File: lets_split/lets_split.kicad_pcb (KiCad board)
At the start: 2 copper layers, 113 x 82 mm, 64 parts, among them P1 USB-rewire, P2 USB_OTG, P3 WS2812-Strip, P4 TRRS jack, SW1 SW_PUSH, SW10 SW_PUSH, SW11 SW_PUSH, SW12 SW_PUSH, SW13 SW_PUSH, SW14 SW_PUSH, SW15 SW_PUSH, SW16 SW_PUSH, SW17 SW_PUSH, SW18 SW_PUSH, SW19 SW_PUSH, SW2 SW_PUSH, SW20 SW_PUSH, SW21 SW_PUSH, SW22 SW_PUSH, SW23 SW_PUSH, SW24 SW_PUSH, SW3 SW_PUSH, SW4 SW_PUSH, SW5 SW_PUSH, SW6 SW_PUSH, SW7 SW_PUSH, SW8 SW_PUSH, SW9 SW_PUSH, U1 ArduinoProMicro

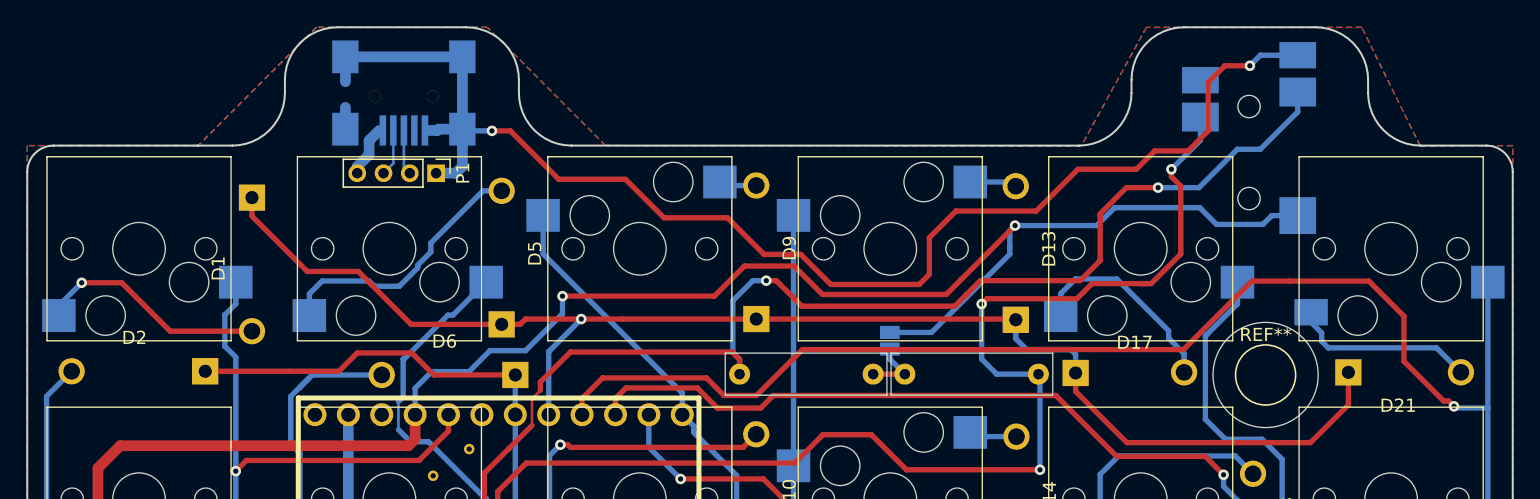
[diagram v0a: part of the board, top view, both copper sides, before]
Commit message: Increased powertraces thickness to TRRS socket
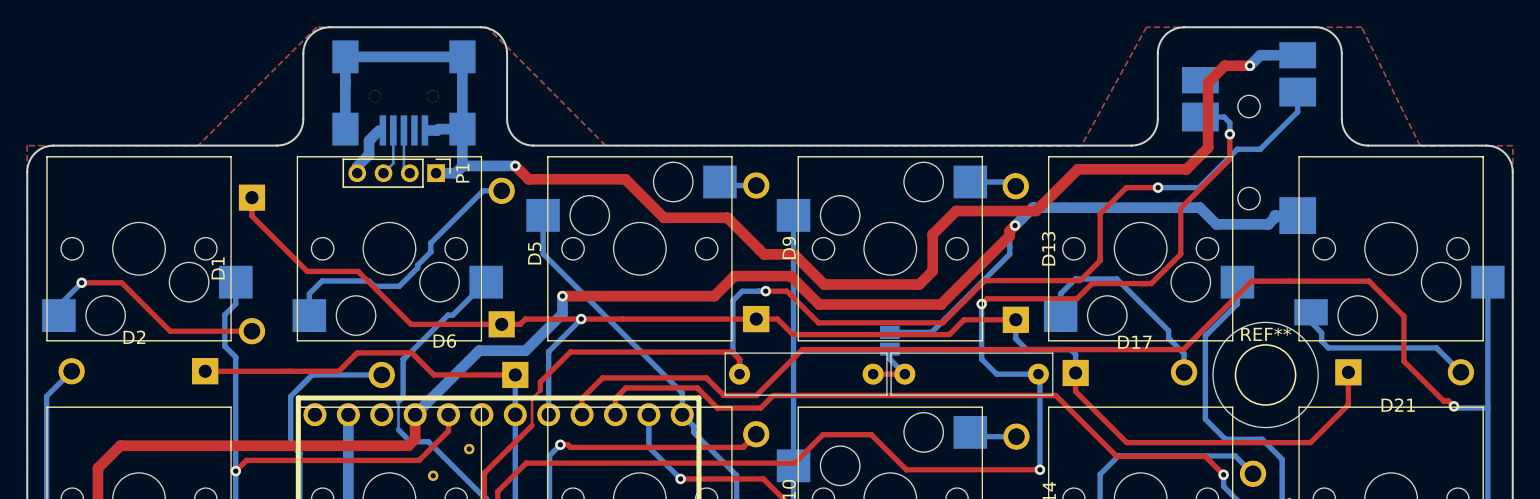
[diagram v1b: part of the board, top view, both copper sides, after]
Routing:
- net SCL/D3: track 99.2 -> 101.5 mm
- net GND: track 143.4 -> 145.2 mm
- net row0: track 106.7 -> 107.7 mm
- net VCC: track 135.3 -> 134.5 mm
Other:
- outline, holes or cut-outs redrawn

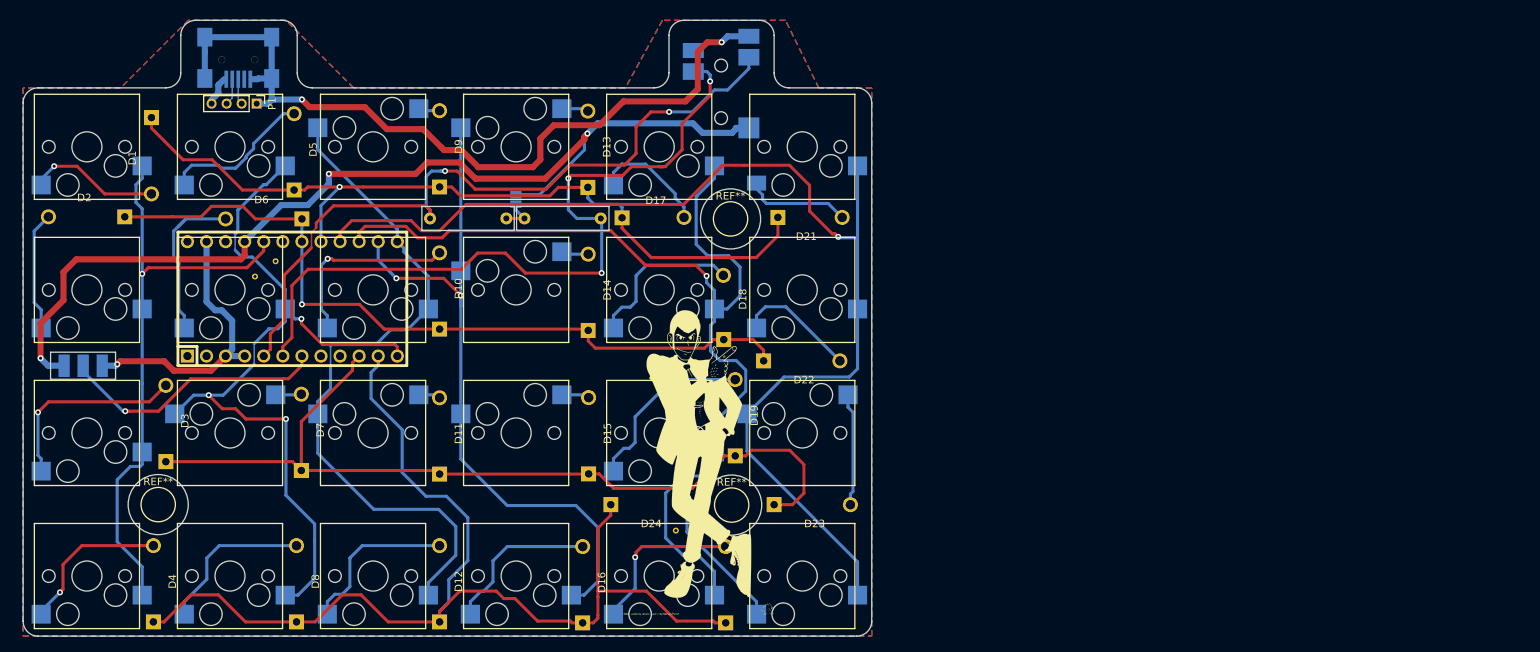
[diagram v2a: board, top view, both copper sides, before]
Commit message: Switched to using diode footprints with actual silk screen, and moved dioes away from socket pads
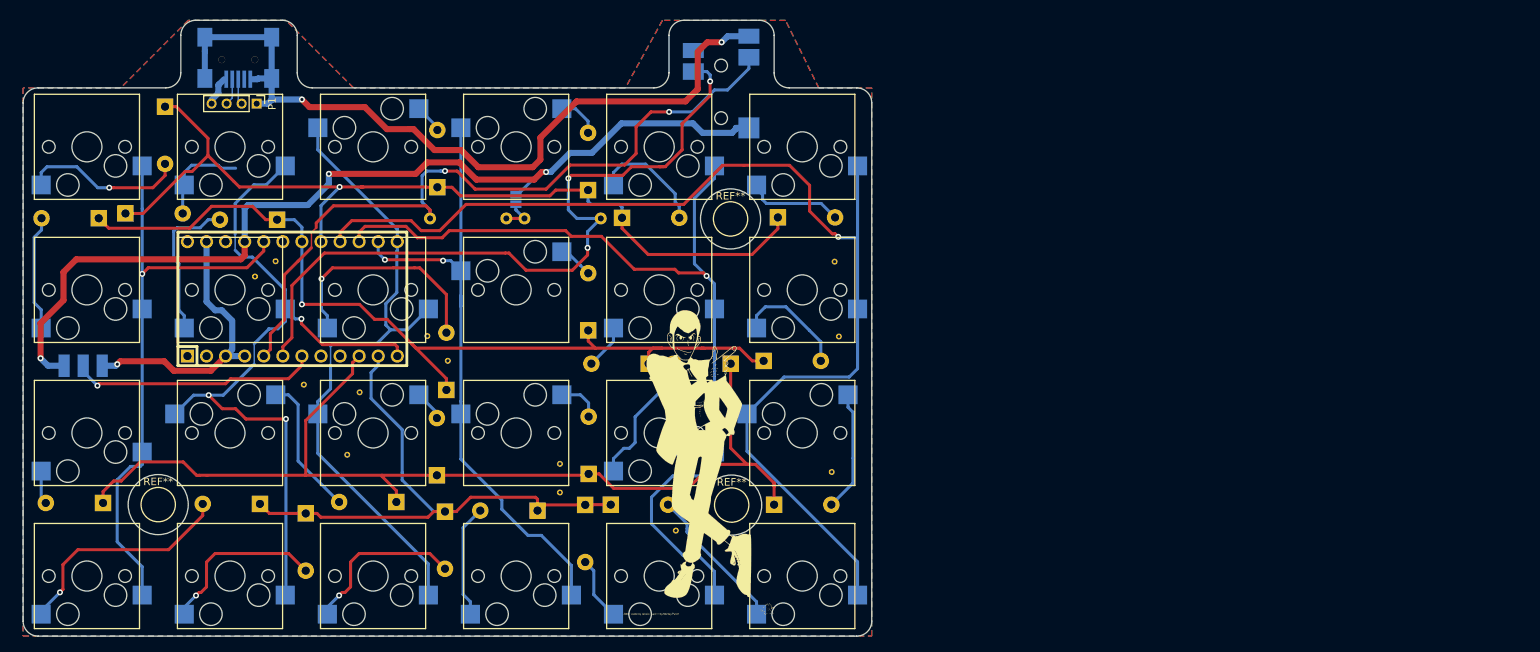
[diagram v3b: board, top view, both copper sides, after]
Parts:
- added REF**: 1pin, Connect:1pin, F.Cu at (135.8, 98.0)
- added REF**: 1pin, Connect:1pin, F.Cu at (153.5, 118.9)
- added REF**: 1pin, Connect:1pin, F.Cu at (190.6, 98.1)
- added REF**: 1pin, Connect:1pin, F.Cu at (138.6, 101.3)
- added REF**: 1pin, Connect:1pin, F.Cu at (119.4, 104.5)
- added REF**: 1pin, Connect:1pin, F.Cu at (126.8, 105.5)
- added REF**: 1pin, Connect:1pin, F.Cu at (125.2, 113.9)
- added REF**: 1pin, Connect:1pin, F.Cu at (189.7, 116.1)
- added REF**: 1pin, Connect:1pin, F.Cu at (190.1, 88.1)
- added REF**: 1pin, Connect:1pin, F.Cu at (153.5, 115.1)
- D1, D10, D11, D12, D13, D14, D15, D16, D17, D18, D19, D2, D20, D21, D22, D23, D24, D3, D4, D5, D6, D7, D8, D9: footprint Diodes_ThroughHole:Diode_DO-41_SOD81_Horizontal_RM10 -> Diodes_ThroughHole:D_DO-41_SOD81_P7.62mm_Horizontal; moved to B.Cu
- P3: footprint SMD_PAD_1x03_Pitch2.54mm -> Wirepads:SMD_PAD_1x03_Pitch2.54mm
- SW6: footprint Kailh-socket -> CherryMX:Kailh-socket
- moved D20 24.4 mm to (156.8, 120.5), turned to 270 degrees
- moved D5 22.7 mm to (95.6, 81.7), turned to 0 degrees
- moved D4 21.2 mm to (113.5, 120.4), turned to 180 degrees
- moved D16 16.1 mm to (150.5, 121.3), turned to 180 degrees
- moved D12 14.7 mm to (138.2, 121.4), turned to 270 degrees
- moved D8 14.5 mm to (119.6, 121.7), turned to 270 degrees
- moved D7 13.3 mm to (131.7, 120.1), turned to 180 degrees
- moved D19 12.3 mm to (176.2, 101.7), turned to 180 degrees
- moved D18 10.5 mm to (165.3, 101.7), turned to 180 degrees
- moved D3 10.0 mm to (92.6, 120.3), turned to 180 degrees
- moved D10 8.15 mm to (138.4, 105.2)
- moved D2 3.47 mm to (92.1, 82.4)
- moved D6 3.30 mm to (115.8, 82.5)
- moved D1 2.33 mm to (100.9, 67.5)
- moved D21 1.60 mm to (182.5, 82.2)
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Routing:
- net row3: track 148.8 -> 76.6 mm
- net Net-(D3-Pad2): track 26.5 -> 4.49 mm, vias 1 -> 0
- net row2: track 116.2 -> 137.8 mm
- net row1: track 103.4 -> 119.5 mm
- net Net-(D18-Pad2): track 21.6 -> 5.96 mm
- net Net-(D7-Pad2): track 3.44 -> 18.8 mm
- net Net-(D20-Pad2): track 21.7 -> 8.51 mm, vias 1 -> 0
- net col4: track 134.1 -> 121.5 mm
- net row0: track 107.7 -> 120.0 mm
- net col3: track 94.4 -> 84.3 mm
- net Net-(D4-Pad2): track 20.9 -> 30.7 mm
- net Net-(D5-Pad2): track 20.4 -> 12.9 mm
- net Net-(D19-Pad2): track 24.2 -> 18.0 mm
- net VCC: track 134.5 -> 128.3 mm
- net Net-(D16-Pad2): track 21.3 -> 15.1 mm
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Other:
- board text removed: "top up"

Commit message: Moved silkscreen around a bit
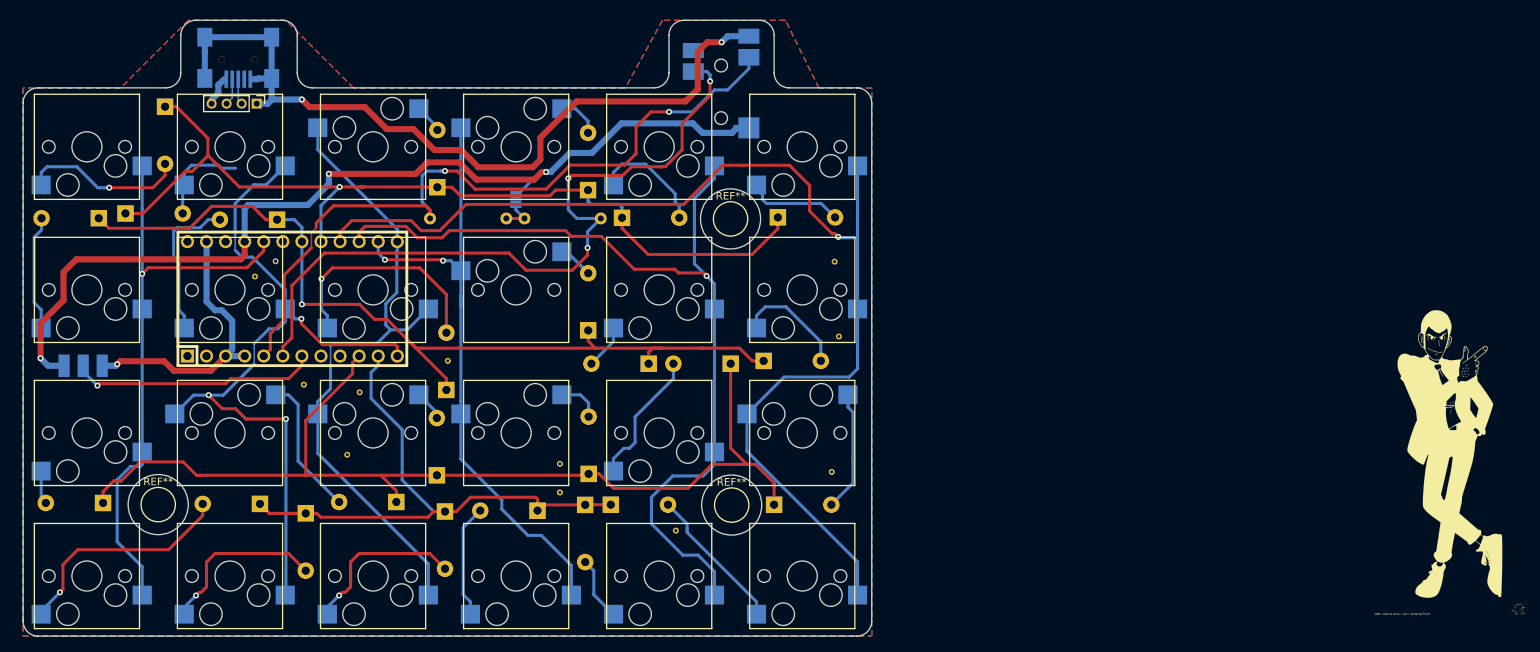
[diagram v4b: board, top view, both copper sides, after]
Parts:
- removed the REF** at (135.8, 98.0)
- moved G*** 100.0 mm to (263.8, 104.0)
- moved G*** 100.0 mm to (272.0, 113.8)

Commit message: Routed board with reversible socket footprint, and mirrored connectors
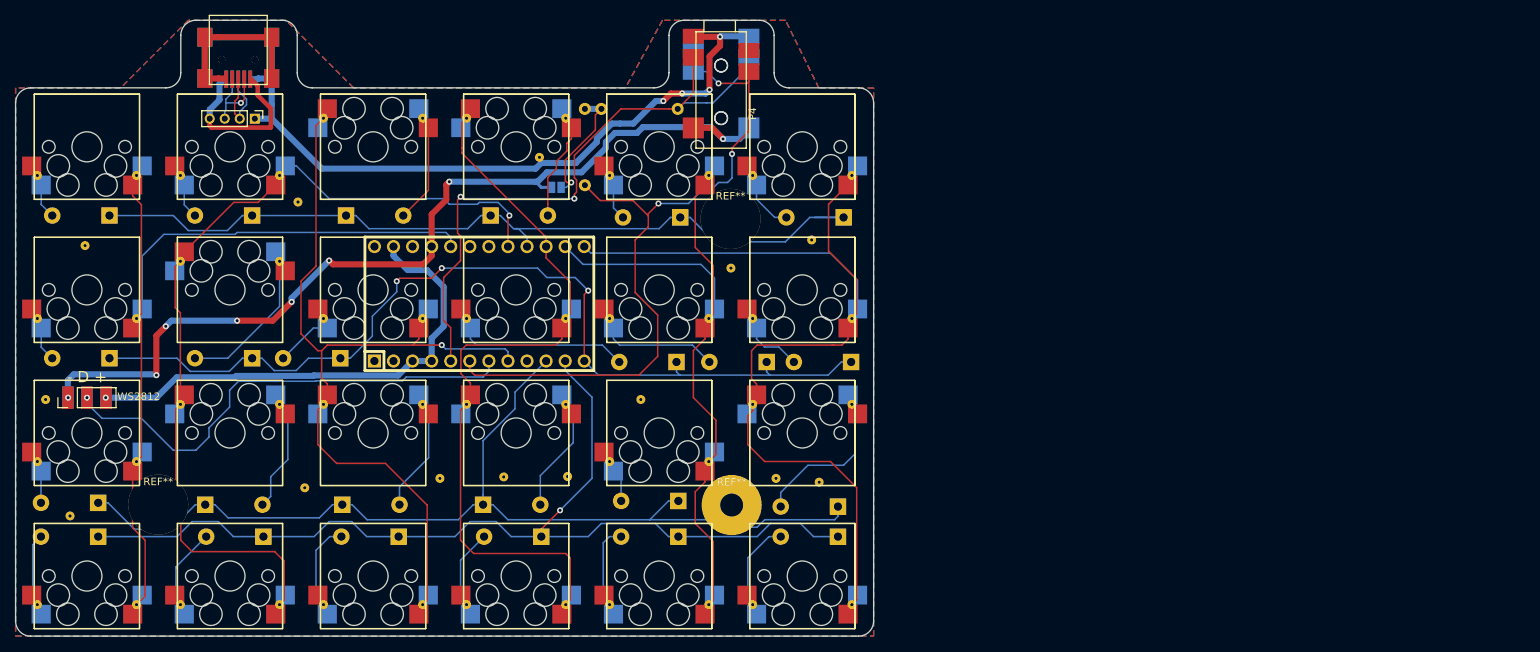
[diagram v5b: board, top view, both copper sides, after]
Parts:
- removed G*** (x2): LOGO, LOGO
- removed the REF** at (190.6, 98.1)
- removed the REF** at (115.6, 88.1)
- removed the REF** at (112.9, 90.1)
- removed the REF** at (168.9, 124.0)
- removed the REF** at (138.6, 101.3)
- removed the REF** at (119.4, 104.5)
- removed the REF** at (126.8, 105.5)
- removed the REF** at (125.2, 113.9)
- removed the REF** at (190.1, 88.1)
- removed the REF** at (153.5, 115.1)
- removed the REF** at (153.5, 118.9)
- added P2: USB_OTG, Connectors:USB-Mini-B-SMD, F.Cu at (110.7, 60.0)
- added P3: WS2812, Wirepads:SMD_PAD_1x03_Pitch2.54mm, F.Cu at (88.0, 106.2)
- added P4: TRRS jack, Connectors:SJ-4351X-SMT, F.Cu at (174.9, 65.3)
- added REF**: 1pin, Connect:1pin, F.Cu at (118.6, 80.2)
- added REF**: 1pin, Connect:1pin, F.Cu at (176.2, 89.0)
- added REF**: 1pin, Connect:1pin, F.Cu at (150.8, 74.2)
- added REF**: 1pin, Connect:1pin, F.Cu at (88.2, 122.0)
- added REF**: 1pin, Connect:1pin, F.Cu at (85.0, 106.5)
- added REF**: 1pin, Connect:1pin, F.Cu at (188.0, 117.5)
- added REF**: 1pin, Connect:1pin, F.Cu at (154.5, 116.8)
- added REF**: 1pin, Connect:1pin, F.Cu at (182.2, 117.0)
- added REF**: 1pin, Connect:1pin, F.Cu at (164.2, 106.5)
- added REF**: 1pin, Connect:1pin, F.Cu at (119.5, 118.2)
- added REF**: 1pin, Connect:1pin, F.Cu at (137.5, 117.0)
- added REF**: 1pin, Connect:1pin, F.Cu at (146.0, 116.8)
- added REF**: 1pin, Connect:1pin, F.Cu at (187.0, 85.2)
- P3: value WS2812-Strip -> WS2812
- SW1, SW10, SW11, SW12, SW13, SW14, SW15, SW16, SW17, SW18, SW19, SW2, SW20, SW21, SW22, SW23, SW24, SW3, SW4, SW5, SW6, SW7, SW8, SW9: footprint CherryMX:Kailh-socket -> CherryMX:Kailh-socket-mirrorable
- moved REF** 103.9 mm to (90.2, 86.0)
- moved D24 30.5 mm to (190.5, 124.8), turned to 180 degrees
- moved D7 25.5 mm to (106.2, 120.5), turned to 0 degrees
- moved U1 24.9 mm to (142.8, 93.8)
- moved D4 22.0 mm to (92.0, 124.8)
- moved D19 19.6 mm to (169.2, 120.0)
- moved R1 19.3 mm to (159.0, 67.8), turned to 0 degrees
- moved D6 18.7 mm to (112.5, 101.0)
- moved D2 18.7 mm to (93.5, 101.0)
- moved D5 16.9 mm to (112.5, 82.0), turned to 180 degrees
- moved R2 16.7 mm to (156.8, 67.8), turned to 270 degrees
- moved D1 16.3 mm to (93.5, 82.0), turned to 180 degrees
- moved D18 15.7 mm to (181.0, 101.5)
- moved D10 14.7 mm to (124.2, 101.0), turned to 180 degrees
- moved D15 14.6 mm to (143.2, 120.5), turned to 0 degrees
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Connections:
- P2 pad 4: Net-(P2-Pad4) -> (no net)
- P4 pad 6: Net-(P4-Pad6) -> (no net)
- U1 pad 12: col1 -> row1
- U1 pad 13: col2 -> col5
- U1 pad 14: col3 -> col4
- U1 pad 15: col4 -> col3
- U1 pad 16: col5 -> row0
- U1 pad 17: row0 -> col1
- U1 pad 18: row1 -> Net-(U1-Pad18)
- U1 pad 8: Net-(U1-Pad8) -> col2
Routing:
- net row3: track 76.6 -> 134.0 mm, vias 0 -> 1
- net GND: track 145.3 -> 199.1 mm, vias 3 -> 5
- net col0: track 79.4 -> 119.2 mm, vias 1 -> 0
- net Net-(P3-Pad2): track 33.0 -> 64.6 mm
- net col2: track 87.2 -> 118.5 mm, vias 0 -> 1
- net col4: track 121.5 -> 97.2 mm, vias 1 -> 0
- net col3: track 84.3 -> 107.8 mm, vias 2 -> 0
- net col1: track 103.2 -> 124.5 mm, vias 3 -> 1
- net Net-(D14-Pad2): track 4.69 -> 25.6 mm
- net col5: track 155.4 -> 134.7 mm, vias 1 -> 0
- net Net-(D10-Pad2): track 30.7 -> 10.6 mm, vias 1 -> 0
- net Net-(P1-Pad4): track 4.22 -> 23.4 mm
- net Net-(D4-Pad2): track 30.7 -> 12.8 mm, vias 1 -> 0
- net SDA: track 99.2 -> 82.3 mm
- net Net-(D11-Pad2): track 4.11 -> 18.4 mm
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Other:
- board size 113 x 82 mm -> 114.2 x 82 mm
- net class Default: clearance 0.1524 -> 0.2032; trace_width 0.1524 -> 0.2032
- rule trace_clearance: 0.1524 -> 0.2032

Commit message: Added images of reversible version
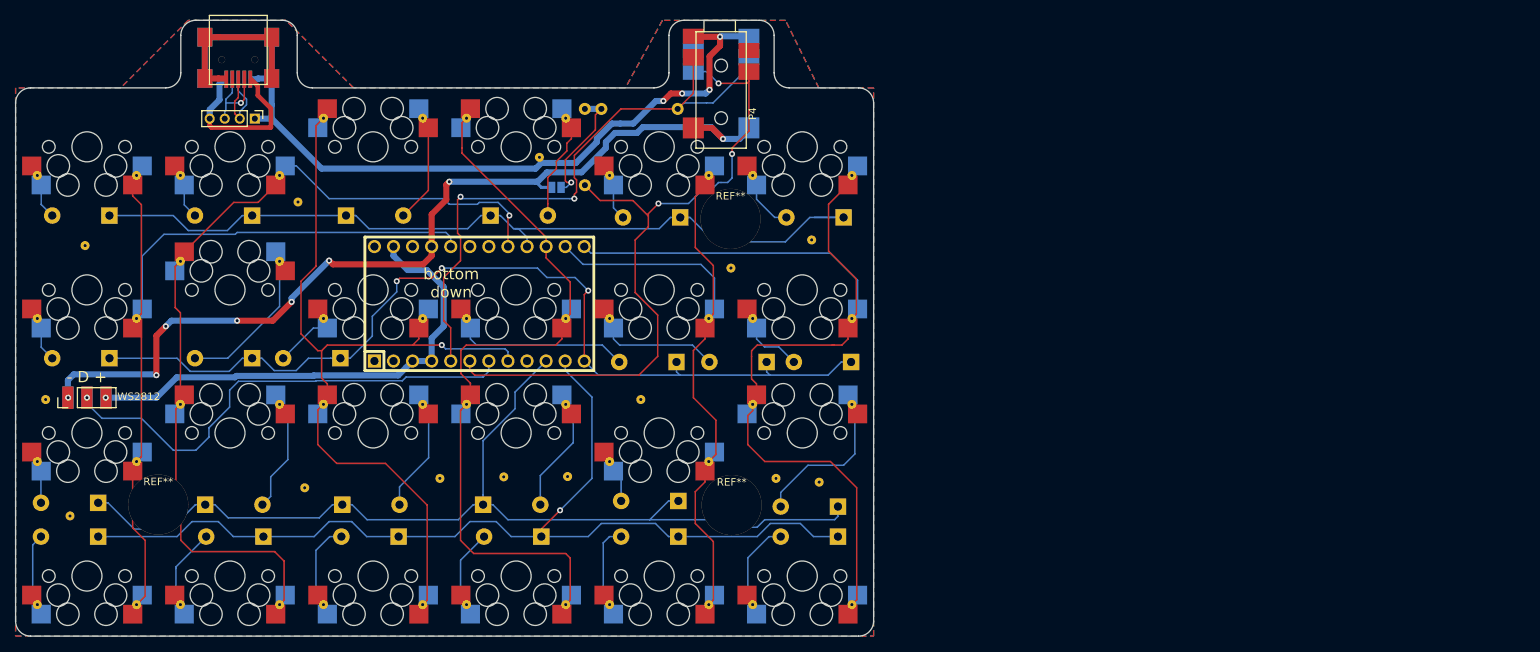
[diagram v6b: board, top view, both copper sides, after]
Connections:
- P2 pad 4: (no net) -> Net-(P2-Pad4)
- P4 pad 6: (no net) -> Net-(P4-Pad6)
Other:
- net class Default: trace_width 0.2032 -> 0.25
- board text added: "bottom down"
